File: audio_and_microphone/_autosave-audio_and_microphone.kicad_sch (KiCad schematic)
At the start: 23 parts, among them J10 Conn_01x02_Pin, J4 Conn_01x03_Pin, J5 Conn_01x02, J7 Conn_01x02, U6 ${SIM.PARAMS}

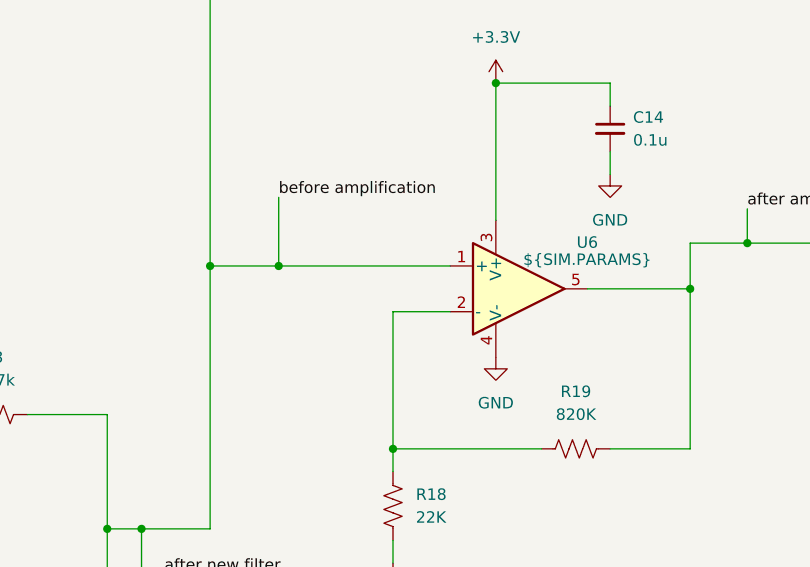
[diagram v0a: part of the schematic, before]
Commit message: added additional testing point and more silkscreen texts
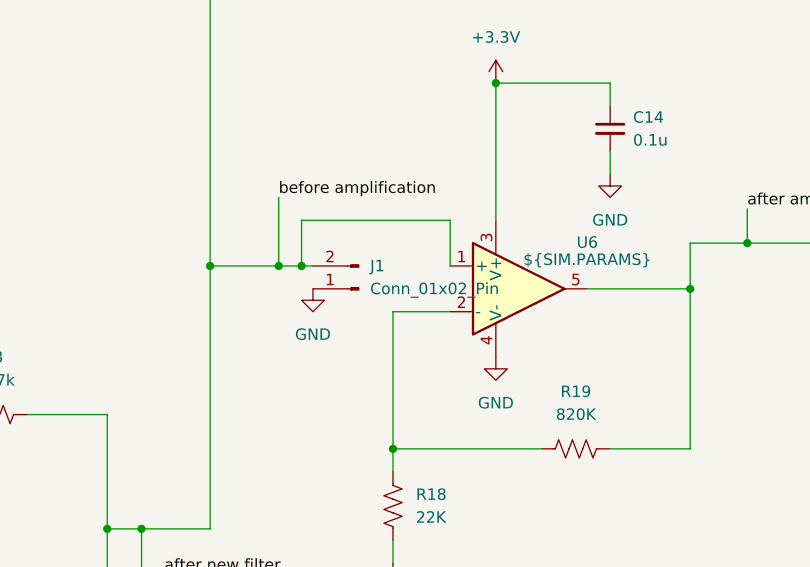
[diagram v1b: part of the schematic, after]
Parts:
- added J1: Conn_01x02_Pin, Connector_PinHeader_2.54mm:PinHeader_1x02_P2.54mm_Vertical, symbol Connector:Conn_01x02_Pin
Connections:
- net GND: now also J1.1 (Pin_1)
- net after new filter: now also J1.2 (Pin_2)
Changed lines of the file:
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@@
 	)
 	(junction
+		(at 167.64 102.87)
+		(diameter 0)
+		(color 0 0 0 0)
+	)
+	(junction
 		(at 189.23 82.55)
 		(diameter 0)
@@
 	(wire
 		(pts
+			(xy 184.15 102.87) (xy 184.15 97.79)
+		)
+		(stroke
+			(width 0)
+			(type default)
+		)
+	)
+	(wire
+		(pts
 			(xy 184.15 107.95) (xy 177.8 107.95)
 		)
@@
 	(wire
 		(pts
+			(xy 184.15 97.79) (xy 167.64 97.79)
+		)
+		(stroke
+			(width 0)
+			(type default)
+		)
+	)
+	(wire
+		(pts
 			(xy 210.82 123.19) (xy 210.82 105.41)
 		)
@@
 	(wire
 		(pts
+			(xy 167.64 102.87) (xy 168.91 102.87)
+		)
+		(stroke
+			(width 0)
+			(type default)
+		)
+	)
+	(wire
+		(pts
 			(xy 119.38 53.34) (xy 119.38 59.69)
 		)
@@
 	(wire
 		(pts
-			(xy 165.1 102.87) (xy 184.15 102.87)
+			(xy 165.1 102.87) (xy 167.64 102.87)
 		)
 		(stroke
@@
 	(wire
 		(pts
+			(xy 167.64 97.79) (xy 167.64 102.87)
+		)
+		(stroke
+			(width 0)
+			(type default)
+		)
+	)
+	(wire
+		(pts
 			(xy 91.44 132.08) (xy 93.98 132.08)
 		)
@@
 	)
 	(symbol
+		(lib_id "power:GND")
+		(at 168.91 105.41 0)
+		(unit 1)
+		(exclude_from_sim no)
+		(in_bom yes)
+		(on_board yes)
+		(dnp no)
+		(fields_autoplaced yes)
+		(property "Reference" "#PWR013"
+			(at 168.91 111.76 0)
+			(effects
+				(font
+					(size 1.27 1.27)
+				)
+				(hide yes)
+			)
+		)
+		(property "Value" "GND"
+			(at 168.91 110.49 0)
+			(effects
+				(font
+					(size 1.27 1.27)
+				)
+			)
+		)
+		(property "Footprint" ""
+			(at 168.91 105.41 0)
+			(effects
+				(font
+					(size 1.27 1.27)
+				)
+				(hide yes)
+			)
+		)
+		(property "Datasheet" ""
+			(at 168.91 105.41 0)
+			(effects
+				(font
+					(size 1.27 1.27)
+				)
+				(hide yes)
+			)
+		)
+		(property "Description" "Power symbol creates a global label with name \"GND\" , ground"
+			(at 168.91 105.41 0)
+			(effects
+				(font
+					(size 1.27 1.27)
+				)
+				(hide yes)
+			)
+		)
+		(pin "1"
+		)
+		(instances
+			(project "audio_and_microphone"
+				(path "/6041ce46-c287-4741-ac80-b7b1d4df1348"
+					(reference "#PWR013")
+					(unit 1)
+				)
+			)
+		)
+	)
+	(symbol
 		(lib_id "Connector:Conn_01x03_Pin")
 		(at 38.1 110.49 0)
@@
 					(unit 1)
 				)
+			)
+		)
+	)
+	(symbol
+		(lib_id "Connector:Conn_01x02_Pin")
+		(at 173.99 105.41 180)
+		(unit 1)
+		(exclude_from_sim no)
+		(in_bom yes)
+		(on_board yes)
+		(dnp no)
+		(fields_autoplaced yes)
+		(property "Reference" "J1"
+			(at 175.26 102.8699 0)
+			(effects
+				(font
+					(size 1.27 1.27)
+				)
+				(justify right)
+			)
+		)
+		(property "Value" "Conn_01x02_Pin"
+			(at 175.26 105.4099 0)
+			(effects
+				(font
+					(size 1.27 1.27)
+				)
+				(justify right)
+			)
+		)
+		(property "Footprint" "Connector_PinHeader_2.54mm:PinHeader_1x02_P2.54mm_Vertical"
+			(at 173.99 105.41 0)
+			(effects
+				(font
+					(size 1.27 1.27)
+				)
+				(hide yes)
+			)
+		)
+		(property "Datasheet" "~"
+			(at 173.99 105.41 0)
+			(effects
+				(font
+					(size 1.27 1.27)
+				)
+				(hide yes)
+			)
+		)
+		(property "Description" "Generic connector, single row, 01x02, script generated"
+			(at 173.99 105.41 0)
+			(effects
+				(font
+					(size 1.27 1.27)
+				)
+				(hide yes)
+			)
+		)
+		(pin "1"
+		)
+		(pin "2"
+		)
+		(instances
+			(project "audio_and_microphone"
+				(path "/6041ce46-c287-4741-ac80-b7b1d4df1348"
+					(reference "J1")
+					(unit 1)
+				)
